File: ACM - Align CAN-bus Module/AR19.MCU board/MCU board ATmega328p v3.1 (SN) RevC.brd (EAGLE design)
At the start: 32 x 25 mm, 50 parts, among them IC1 ATMEGA328P-MMH, IC2 MIC5239-5.0YS_TR, IC3 MCP25625-E_ML, J1 AVR_SPI_PROG_3X2NS, U1 CSTNE16M0V530000R0, U2 CSTNE16M0V530000R0

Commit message: Removed GND from Oscillator. Added new ACM library
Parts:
- moved CANH 5.08 mm to (0.00, 6.15)
- moved CANL 5.08 mm to (0.00, 8.69)
- moved PWM0 5.08 mm to (0.00, 13.8)
- moved PWM1_INT1 5.08 mm to (0.00, 11.2)
- moved C9 2.83 mm to (22.8, 15.9), turned to 180 degrees
- moved U2 2.79 mm to (25.2, 14.0)
- moved C3 1.87 mm to (27.3, 15.9), turned to 0 degrees
- moved C1 0.32 mm to (22.2, 18.7)
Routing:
- net CANL: track 9.93 -> 5.80 mm, vias 1 -> 0
- net GND: track 9.17 -> 12.8 mm, vias 0 -> 12
- net I/O_D2_INT: track 30.2 -> 27.6 mm
- net MCU_OSC2: track 7.60 -> 5.14 mm
- net CANH: track 8.60 -> 6.17 mm, vias 1 -> 0
- net VOLTAGE_CHECK: track 22.4 -> 20.9 mm
- net N$2: track 23.5 -> 22.7 mm
- net 5V: track 61.2 -> 60.5 mm
- net MISO: track 35.9 -> 35.3 mm
- added copper zone on layer 1, net EMPTY
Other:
- board text added: "*Made on Earth by humans*"
- board text added: "+"
- board text removed: "Sponsored by JLC PCB"

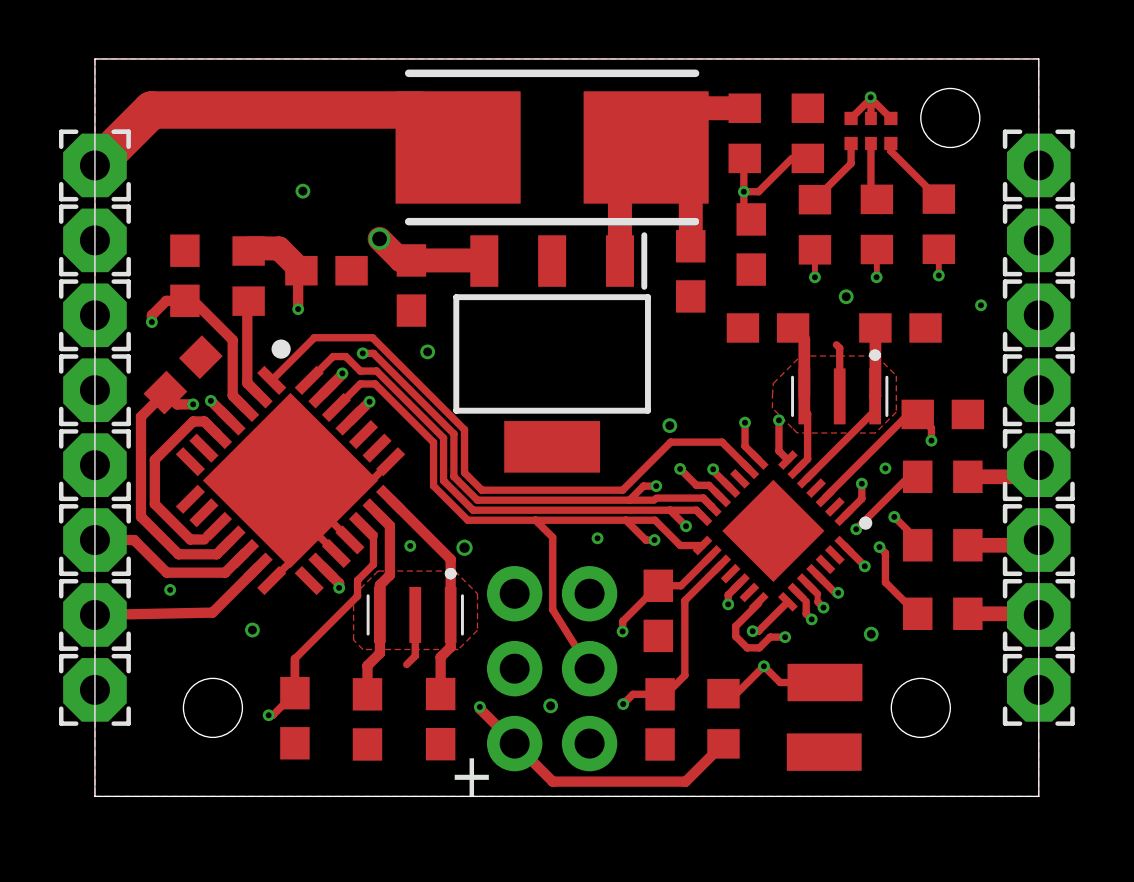
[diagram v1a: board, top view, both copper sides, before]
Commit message: Moved PWM pins away from under oscillator
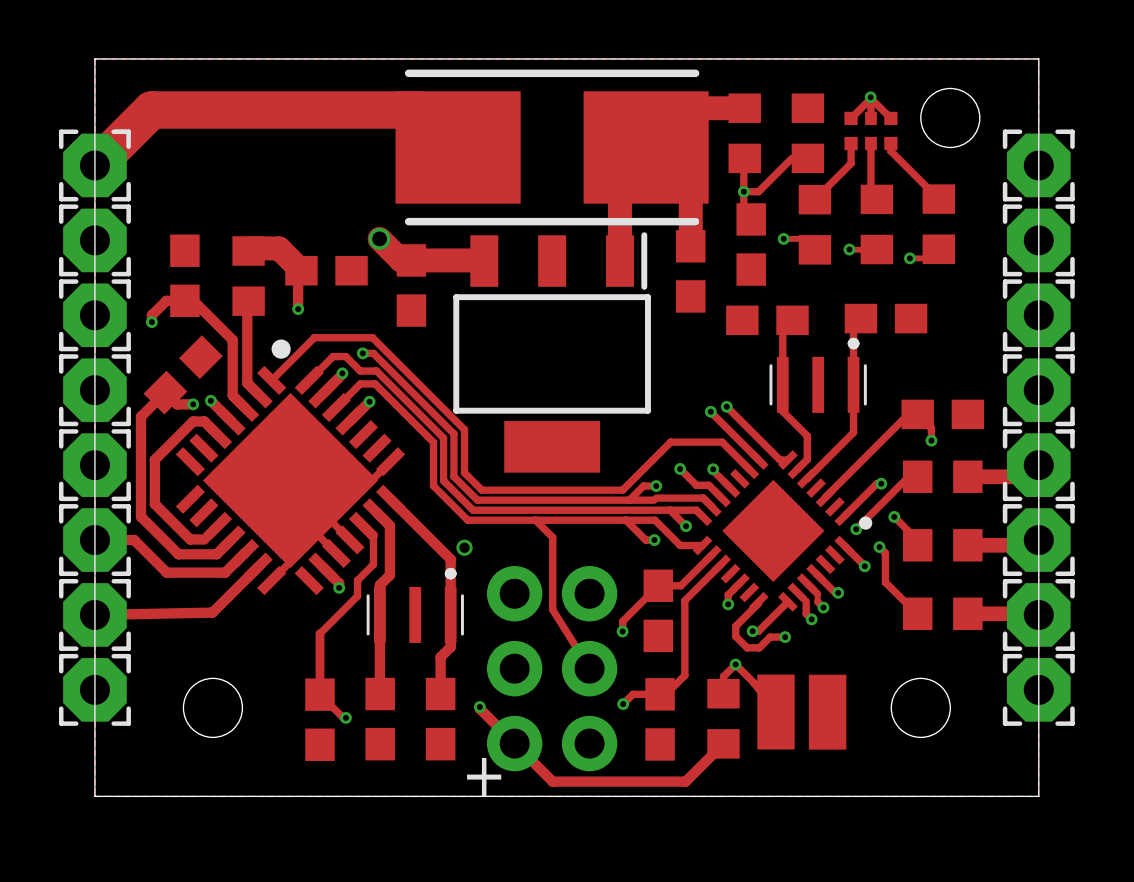
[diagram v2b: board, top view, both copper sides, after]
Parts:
- moved RES_PAD1 1.94 mm to (23.1, 2.86), turned to 0 degrees
- moved RES_PAD2 1.36 mm to (24.8, 2.85), turned to 0 degrees
- moved C7 0.85 mm to (7.63, 2.60)
- moved U2 0.83 mm to (24.5, 14.4)
- moved C3 0.59 mm to (26.8, 16.2)
- moved C2 0.43 mm to (9.67, 2.62)
- moved C9 0.26 mm to (22.8, 16.1)
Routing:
- net GND: track 12.8 -> 9.17 mm, vias 12 -> 0
- net RED_LED: track 8.64 -> 12.1 mm
- net I/O_ADC3: track 15.7 -> 13.1 mm
- net GREEN_LED: track 8.30 -> 10.4 mm
- net BLUE_LED: track 12.2 -> 14.1 mm
- net I/OADC2: track 16.6 -> 15.3 mm
- net I/O_D2_INT: track 27.6 -> 28.6 mm
- net RESET_MCU: track 16.2 -> 15.4 mm
- net 5V: track 60.5 -> 59.8 mm
- net MCU_OSC2: track 5.14 -> 5.68 mm
- removed copper zone on layer 1, net EMPTY
